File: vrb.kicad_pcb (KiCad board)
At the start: 4 copper layers, 75 x 75 mm, 201 parts, among them J1 SM04B-GHS, J10 MiniFit, J11 XT30, J12 Mezzanine, J2 SM04B-GHS, J3 MiniFit, J4 MiniFit, J5 Pixhawk 1, J6 Pixhawk 2, J7 SM04B-GHS, J8 DEBUG, J9 SM04B-GHS, Q1 Q_NMOS_GSD, Q2 Q_NMOS_GSD, U1 STM32G0B1CBUx, U10 INA169, U11 TJA1051TK/3/1J, U12 I3A4W008A033V-001-R, U13 INA169, U14 TPS2121, U15 TPS2121, U16 TLV71333PDQN, U17 TA2528, U18 TPS2116DRL, U2 TJA1051TK/3/1J, U3 LMR51635, U4 INA169, U5 LMR51635, U6 INA169, U7 LMR51635, U8 INA169, U9 LMR51635, Y1 XRCGB16M000FXN20R0

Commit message: finish layout
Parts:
- added D20: RED, LED_SMD:LED_0603_1608Metric, F.Cu at (120.4, 128.4)
- added R78: 330, Resistor_SMD:R_0402_1005Metric, F.Cu at (119.9, 129.8)
- U11, U2: footprint Package_DFN_QFN:DFN-8-1EP_3x3mm_P0.65mm_EP1.55x2.4mm -> Package_SON:HVSON-8-1EP_3x3mm_P0.65mm_EP1.6x2.4mm
- U16: value TLV71333PDQN -> TLV71333PDBVR
- moved D16 2.84 mm to (109.7, 64.5)
- moved D15 2.78 mm to (89.4, 64.9)
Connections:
- C38 pad 1: Net-(U1-VBAT) -> +3V3
- C39 pad 1: Net-(U1-VBAT) -> +3V3
- U1 pad 29: unconnected-(U1-PA9/UCPD1_DBCC1-Pad29) -> /FAULT
- U1 pad 4: Net-(U1-VBAT) -> +3V3
- U1 pad 6: Net-(U1-VBAT) -> +3V3
- U16 pad 1: +3V3 -> +5V
- U16 pad 4: +5V -> unconnected-(U16-NC-Pad4)
- U16 pad 5: GND -> +3V3
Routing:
- net +3V3: track 21.7 -> 271.5 mm, vias 16 -> 24
- net +5V: track 14.7 -> 69.5 mm, vias 4 -> 5
- net VBUS1: track 20.2 -> 64.1 mm, vias 4 -> 6
- net /I2C3_SDA_SMBUS: track 77.4 -> 112.6 mm
- net /I2C3_SCL_SMBUS: track 79.7 -> 110.8 mm, vias 4 -> 3
- net VBUS2: track 6.01 -> 30.1 mm
- net /FAULT: track 0.00 -> 8.18 mm
- net Net-(U1-VBAT): track 6.41 -> 0.00 mm, vias 2 -> 0
- net GND: track 98.4 -> 104.5 mm, vias 131 -> 142
- net /FMU2_VOUT: track 11.4 -> 17.3 mm, vias 6 -> 8
- net Net-(U17-DECAP): track 1.95 -> 7.69 mm
- net Net-(D20-K): track 0.00 -> 1.51 mm
- net /CANFD 2 (Redundant)/FDCAN_N: track 23.2 -> 21.9 mm, vias 6 -> 4
- net /CANFD 1 (Primary)/FDCAN_N: track 23.2 -> 21.9 mm, vias 6 -> 4
- net /SWDIO: track 5.44 -> 6.31 mm
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- added copper zone on F.Cu, net +3V3
- added copper zone on B.Cu, net +BATT
- added copper zone on In2.Cu, net +BATT
- added copper zone on In2.Cu, net /CM_VOUT
- added copper zone on In2.Cu, net /FMU1_VOUT
- added copper zone on In2.Cu, net /FMU2_VOUT
- added copper zone on In2.Cu, net /RADAR_VOUT
- added copper zone on B.Cu, net /RADIO_VOUT
- added copper zone on In2.Cu, net /RADIO_VOUT
- added copper zone on In2.Cu, net /RC Radio/VOUT
- added copper zone on In2.Cu, net /Telemetry Radio/VOUT
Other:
- board text added: "BATT"
- board text added: "COMPUTE"
- board text added: "Fault"
- board text added: "RC"
- board text added: "TELEM"
- board text removed: "FMU 1"
- board text removed: "FMU 2"

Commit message: finish layout
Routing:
- net /I2C3_SCL_SMBUS: track 110.8 -> 134.7 mm, vias 3 -> 4
- net /I2C3_SDA_SMBUS: track 112.6 -> 135.1 mm, vias 4 -> 5
- net +3V3: track 271.5 -> 272.3 mm
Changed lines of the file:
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@@
 	)
 	(segment
+		(start 128.8 119.4)
+		(end 128.8 120.2)
+		(width 0.35)
+		(layer "In2.Cu")
+		(net 3)
+	)
+	(segment
 		(start 117 127.95)
 		(end 119.1 127.95)
@@
 	)
 	(segment
+		(start 100.475 65.975)
+		(end 100.5 65.95)
+		(width 0.15)
+		(layer "F.Cu")
+		(net 89)
+	)
+	(segment
+		(start 100.475 68.1)
+		(end 100.475 65.975)
+		(width 0.15)
+		(layer "F.Cu")
+		(net 89)
+	)
+	(segment
 		(start 134 123.8)
 		(end 135.29 123.8)
@@
 		(net 89)
 	)
+	(via
+		(at 100.475 65.95)
+		(size 0.5)
+		(drill 0.25)
+		(layers "F.Cu" "B.Cu")
+		(net 89)
+	)
 	(segment
 		(start 119.875 67.625)
@@
 	)
 	(segment
+		(start 117.2 64.4)
+		(end 114.95 64.4)
+		(width 0.15)
+		(layer "B.Cu")
+		(net 89)
+	)
+	(segment
 		(start 125.425 70.9)
 		(end 126.75 72.225)
@@
 	)
 	(segment
+		(start 118.5 65.7)
+		(end 117.2 64.4)
+		(width 0.15)
+		(layer "B.Cu")
+		(net 89)
+	)
+	(segment
 		(start 132.226 87.301)
 		(end 132.226 88.924)
@@
 	)
 	(segment
+		(start 114.95 64.4)
+		(end 113.4 65.95)
+		(width 0.15)
+		(layer "B.Cu")
+		(net 89)
+	)
+	(segment
+		(start 120.975 65.7)
+		(end 118.5 65.7)
+		(width 0.15)
+		(layer "B.Cu")
+		(net 89)
+	)
+	(segment
 		(start 119.875 70.925)
 		(end 120.625 71.675)
@@
 	)
 	(segment
+		(start 113.4 65.95)
+		(end 100.475 65.95)
+		(width 0.15)
+		(layer "B.Cu")
+		(net 89)
+	)
+	(segment
 		(start 132.226 88.924)
 		(end 131.275 89.875)
@@
 	)
 	(segment
+		(start 98.475 68.1)
+		(end 98.475 66.375)
+		(width 0.15)
+		(layer "F.Cu")
+		(net 90)
+	)
+	(segment
 		(start 130.853986 130.3)
 		(end 131.575001 131.021015)
@@
 	)
 	(segment
+		(start 98.475 66.375)
+		(end 98.45 66.35)
+		(width 0.15)
+		(layer "F.Cu")
+		(net 90)
+	)
+	(segment
 		(start 135.29 122.8)
 		(end 135.29 122.21)
@@
 	)
 	(via
+		(at 98.45 66.35)
+		(size 0.5)
+		(drill 0.25)
+		(layers "F.Cu" "B.Cu")
+		(net 90)
+	)
+	(via
 		(at 135.3 122.2)
 		(size 0.5)
@@
 	)
 	(segment
+		(start 118.699 66.676)
+		(end 118.975 66.4)
+		(width 0.15)
+		(layer "B.Cu")
+		(net 90)
+	)
+	(segment
 		(start 131.575001 131.021015)
 		(end 135.3 127.296016)
@@
 	)
 	(segment
+		(start 98.776 66.676)
+		(end 118.699 66.676)
+		(width 0.15)
+		(layer "B.Cu")
+		(net 90)
+	)
+	(segment
 		(start 124.426 71.424)
 		(end 123.65 72.2)
@@
 	)
 	(segment
+		(start 98.45 66.35)
+		(end 98.776 66.676)
+		(width 0.15)
+		(layer "B.Cu")
+		(net 90)
+	)
+	(segment
 		(start 119.35 71.125)
 		(end 119.35 67.9)
@@
 		(polygon
 			(pts
-				(xy 132.2 96.3) (xy 132.2 88.1) (xy 135.4 88.1) (xy 135.4 88.1) (xy 137 88.1) (xy 137 96.3)
+				(xy 132.2 96.3) (xy 132.2 88.1) (xy 135.4 88.1) (xy 137 88.1) (xy 137 96.3)
 			)
 		)

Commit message: move to 6 layer
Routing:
- added copper zone on In3.Cu, net +BATT
- added copper zone on In3.Cu, net /CM_VOUT
- added copper zone on In3.Cu, net /FMU1_VOUT
- added copper zone on In3.Cu, net /FMU2_VOUT
- added copper zone on In3.Cu, net /RADAR_VOUT
- added copper zone on In3.Cu, net /RADIO_VOUT
- added copper zone on In3.Cu, net /RC Radio/VOUT
- added copper zone on In3.Cu, net /Telemetry Radio/VOUT
- added copper zone on In4.Cu, net GND
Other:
- copper layers 4 -> 6
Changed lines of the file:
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@@
 		(4 "In1.Cu" signal)
 		(6 "In2.Cu" signal)
+		(8 "In3.Cu" signal)
+		(10 "In4.Cu" signal)
 		(2 "B.Cu" signal)
 		(9 "F.Adhes" user "F.Adhesive")
@@
 			(layer "dielectric 2"
 				(type "core")
-				(thickness 1.24)
+				(thickness 0.535)
 				(material "FR4")
 				(epsilon_r 4.5)
@@
 				(loss_tangent 0.02)
 			)
+			(layer "In3.Cu"
+				(type "copper")
+				(thickness 0.035)
+			)
+			(layer "dielectric 4"
+				(type "core")
+				(thickness 0.535)
+				(material "FR4")
+				(epsilon_r 4.5)
+				(loss_tangent 0.02)
+			)
+			(layer "In4.Cu"
+				(type "copper")
+				(thickness 0.035)
+			)
+			(layer "dielectric 5"
+				(type "prepreg")
+				(thickness 0.1)
+				(material "FR4")
+				(epsilon_r 4.5)
+				(loss_tangent 0.02)
+			)
 			(layer "B.Cu"
 				(type "copper")
@@
 		(net 1)
 		(net_name "GND")
-		(layer "In1.Cu")
+		(layers "In1.Cu" "In4.Cu")
 		(hatch edge 0.5)
 		(priority 15)
@@
 		(net 12)
 		(net_name "/FMU2_VOUT")
-		(layer "In2.Cu")
+		(layers "In2.Cu" "In3.Cu")
 		(name "radio")
 		(hatch edge 0.5)
@@
 		(net 83)
 		(net_name "/RC Radio/VOUT")
-		(layer "In2.Cu")
+		(layers "In2.Cu" "In3.Cu")
 		(name "radio")
 		(hatch edge 0.5)
@@
 		(net 9)
 		(net_name "/FMU1_VOUT")
-		(layer "In2.Cu")
+		(layers "In2.Cu" "In3.Cu")
 		(name "radio")
 		(hatch edge 0.5)
@@
 		(net 23)
 		(net_name "/CM_VOUT")
-		(layer "In2.Cu")
+		(layers "In2.Cu" "In3.Cu")
 		(name "radio")
 		(hatch edge 0.5)
@@
 		(net 21)
 		(net_name "/RADAR_VOUT")
-		(layer "In2.Cu")
+		(layers "In2.Cu" "In3.Cu")
 		(name "radio")
 		(hatch edge 0.5)
@@
 		(net 7)
 		(net_name "+BATT")
-		(layer "In2.Cu")
+		(layers "In2.Cu" "In3.Cu")
 		(hatch edge 0.5)
 		(priority 18)
@@
 		(net 16)
 		(net_name "/RADIO_VOUT")
-		(layer "In2.Cu")
+		(layers "In2.Cu" "In3.Cu")
 		(name "radio")
 		(hatch edge 0.5)
@@
 		(net 12)
 		(net_name "/FMU2_VOUT")
-		(layer "In2.Cu")
+		(layers "In2.Cu" "In3.Cu")
 		(name "radio")
 		(hatch edge 0.5)
@@
 		(net 84)
 		(net_name "/Telemetry Radio/VOUT")
-		(layer "In2.Cu")
+		(layers "In2.Cu" "In3.Cu")
 		(name "radio")
 		(hatch edge 0.5)
@@
 		(net 16)
 		(net_name "/RADIO_VOUT")
-		(layer "In2.Cu")
+		(layers "In2.Cu" "In3.Cu")
 		(name "radio")
 		(hatch edge 0.5)

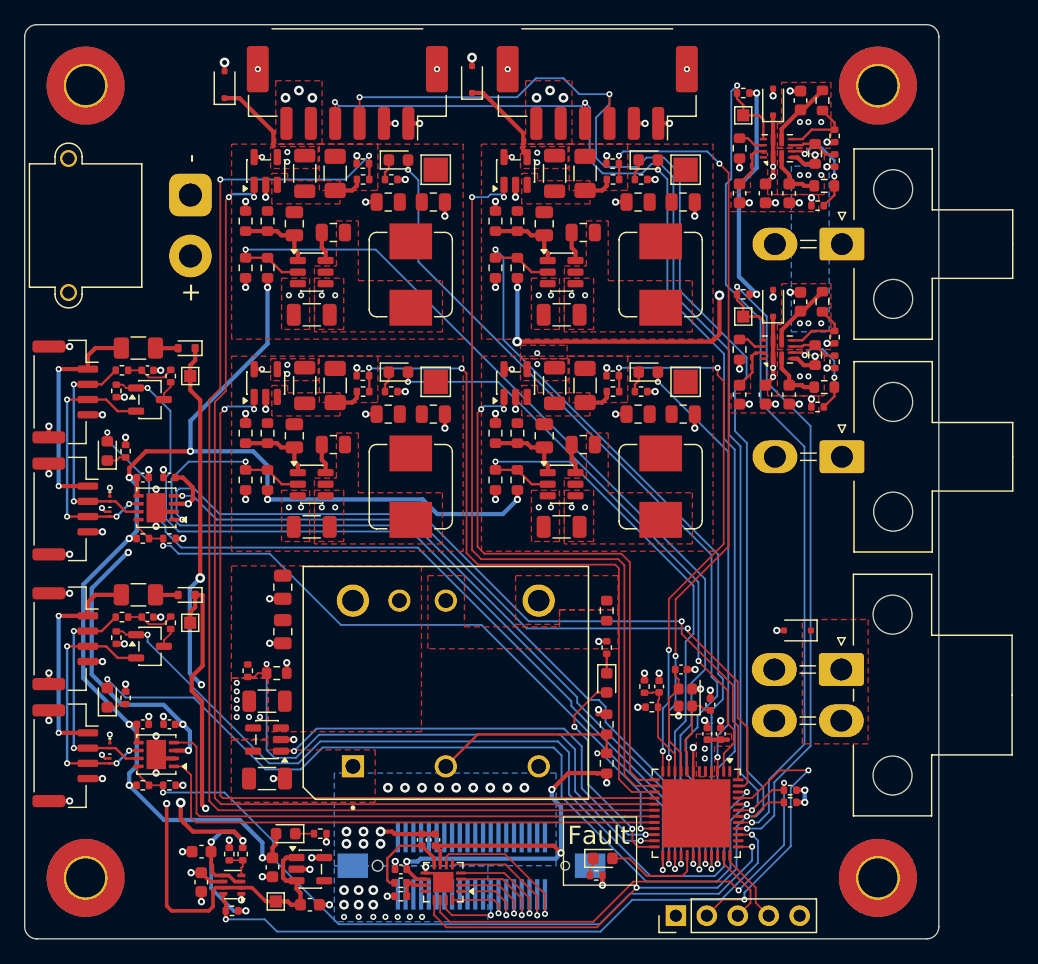
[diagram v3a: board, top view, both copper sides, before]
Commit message: optimize components, update schematic pdf
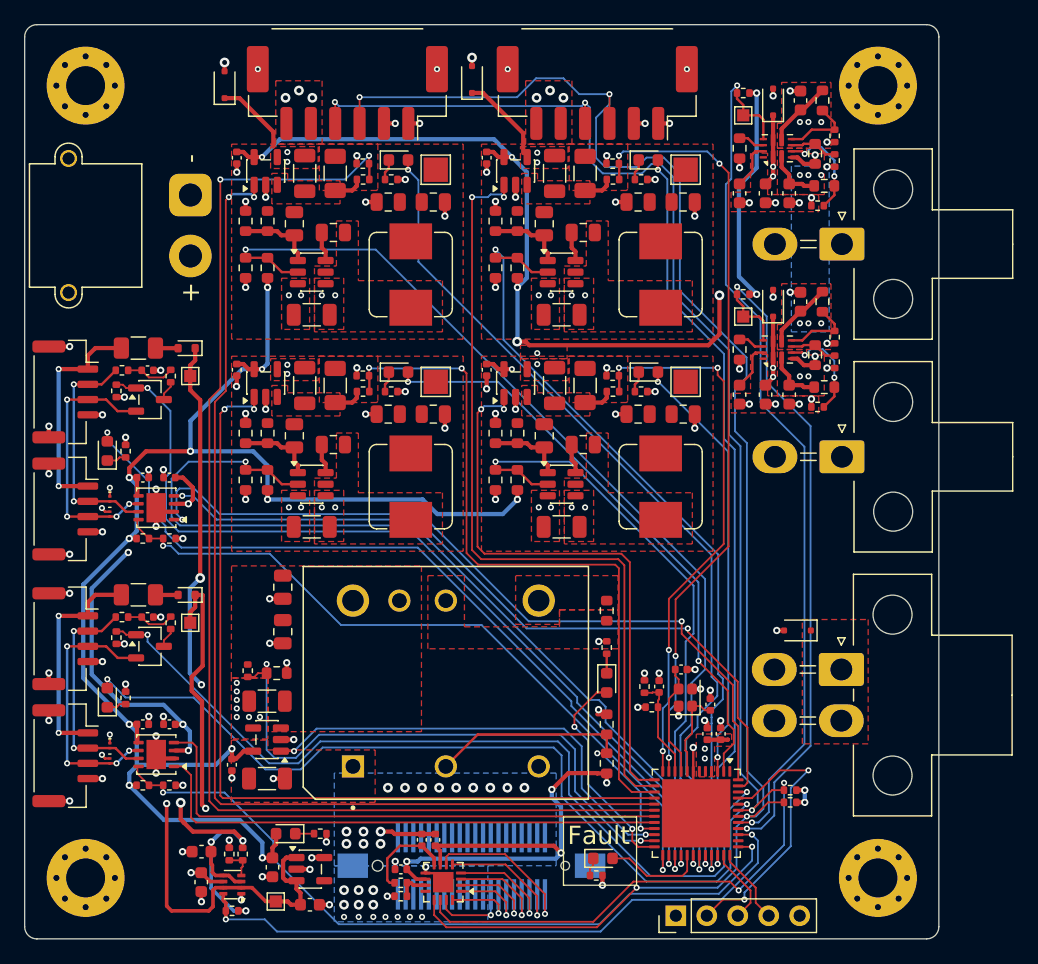
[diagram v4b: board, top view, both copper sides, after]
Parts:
- added C47: 100n, Capacitor_SMD:C_0402_1005Metric, F.Cu at (90.4, 70.9)
- added C48: 100n, Capacitor_SMD:C_0402_1005Metric, F.Cu at (110.9, 70.9)
- added C49: 100n, Capacitor_SMD:C_0402_1005Metric, F.Cu at (110.9, 88.3)
- added C50: 100n, Capacitor_SMD:C_0402_1005Metric, F.Cu at (90.4, 88.3)
- added C51: 100n, Capacitor_SMD:C_0402_1005Metric, F.Cu at (90.0, 120.7)
- H1, H2, H3, H4: footprint MountingHole:MountingHole_3.2mm_M3_Pad_TopBottom -> MountingHole:MountingHole_3.2mm_M3_Pad_Via
- R15, R23, R31, R42, R7: value 1m -> 5m
- U10, U13, U4, U6, U8: value INA169 -> INA180A2
- U17: value TA2528 -> TLA2528
- moved C12 3.70 mm to (127.0, 74.5), turned to 0 degrees
- moved C13 3.70 mm to (123.3, 74.5), turned to 180 degrees
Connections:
- U10 pad 5: +BATT -> +3V3
- U13 pad 5: +BATT -> +3V3
- U4 pad 5: +BATT -> +3V3
- U6 pad 5: +BATT -> +3V3
- U8 pad 5: +BATT -> +3V3
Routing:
- net +3V3: track 272.3 -> 329.4 mm, vias 24 -> 29
- net GND: track 104.5 -> 108.4 mm, vias 142 -> 147
- net +BATT: track 2.60 -> 0.00 mm, vias 25 -> 21

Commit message: added silk screen stuff
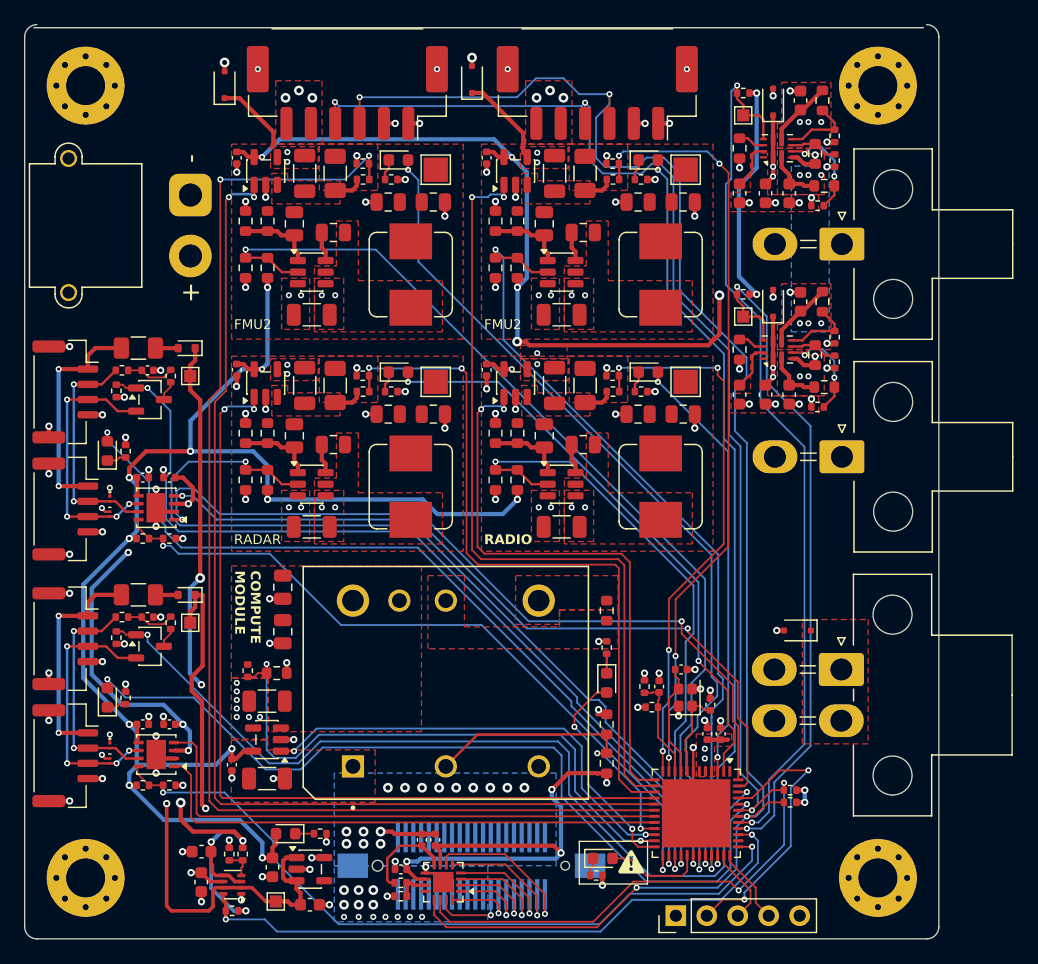
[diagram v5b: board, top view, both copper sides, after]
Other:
- outline, holes or cut-outs redrawn
- board text added: "COMPUTE MODULE"
- board text added: "Designed with in California, USA"
- board text added: "F*CKN'"
- board text added: "FMU2"
- board text added: "RADAR"
- board text added: "RADIO"
- board text added: "READ THE DOCS"
- board text removed: "Fault"
